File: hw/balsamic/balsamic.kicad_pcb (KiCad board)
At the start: 4 copper layers, 17.6 x 28.6 mm, 54 parts, among them J2 AXT524124, J3 USB_B_Micro, U1 BMI270, U2 MAX77651BEWVA+T, U3 ISP1807-LR-RS

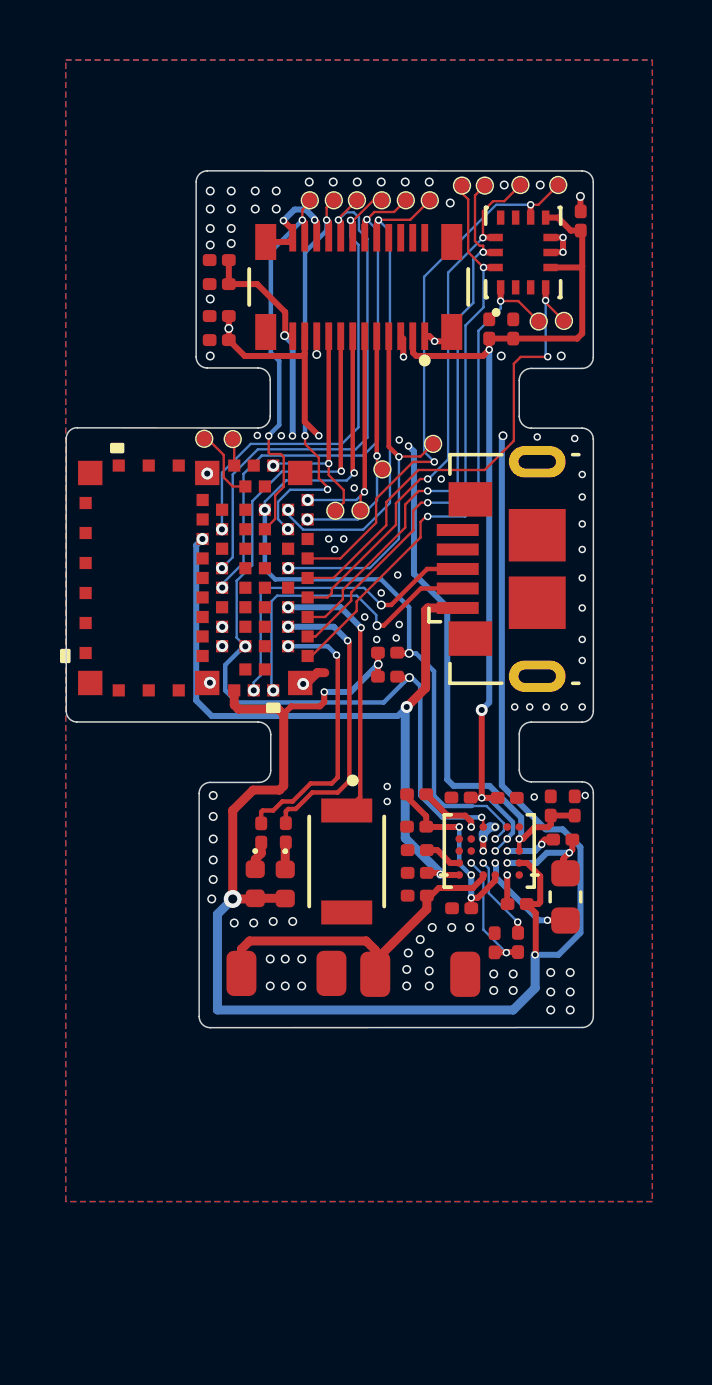
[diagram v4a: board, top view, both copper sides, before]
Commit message: incorporated Malik's board feedback
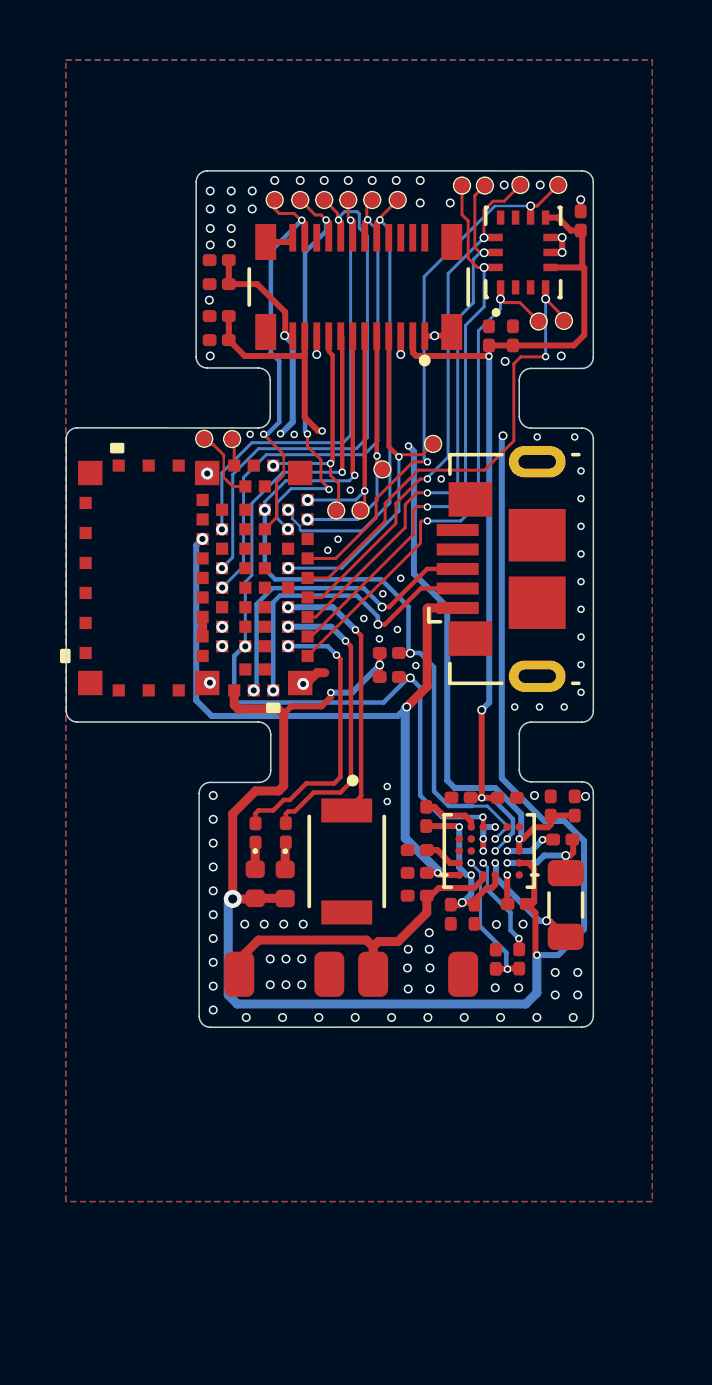
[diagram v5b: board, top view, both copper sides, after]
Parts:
- L1: footprint Inductor_SMD:L_0603_1608Metric -> Inductor_SMD:L_0805_2012Metric
- moved C1 3.50 mm to (76.1, 78.4), turned to -90 degrees
- moved TP17 1.17 mm to (69.5, 54.6)
- moved TP16 1.12 mm to (70.3, 54.6)
- moved TP13 1.12 mm to (72.7, 54.6)
- moved TP14 1.12 mm to (71.9, 54.6)
- moved TP15 1.09 mm to (71.1, 54.6)
- moved TP12 1.07 mm to (73.5, 54.6)
- moved R2 0.81 mm to (74.5, 75.2), turned to 90 degrees
- moved R5 0.55 mm to (77.6, 79.9)
- moved R3 0.55 mm to (76.8, 79.9)
- moved C11 0.41 mm to (75.3, 78.4), turned to -90 degrees
- moved L1 0.27 mm to (79.2, 78.1)
- moved C10 0.23 mm to (77.4, 59.1)
- moved C14 0.23 mm to (76.6, 59.1)
- moved R6 0.19 mm to (68.8, 75.7)
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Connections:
- net nRF_P0_02 renamed IMU_INT1
- net nRF_P0_15 renamed BUTTON
- net nRF_P0_31 renamed IMU_INT2
- U3 pad 20: GND -> Net-(U3-Pad20)
- U3 pad 22: GND -> Net-(U3-Pad20)
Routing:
- net GND: track 10.2 -> 7.30 mm, vias 111 -> 115
- net PMU_VSBB1: track 69.4 -> 68.1 mm, vias 7 -> 6
- net DVP_D3: track 16.4 -> 15.4 mm
- net DVP_D2: track 18.8 -> 17.9 mm
- net Net-(U3-Pad20): track 0.00 -> 0.65 mm
- net PMU_VSBB0: track 29.8 -> 30.5 mm
- net DVP_D1: track 16.1 -> 15.4 mm
- net DVP_MCLK: track 13.1 -> 13.7 mm
- net Net-(R5-Pad2): track 2.81 -> 3.38 mm
- net Net-(R3-Pad1): track 4.27 -> 4.83 mm
- net BATT: track 11.9 -> 11.3 mm
- net DVP_TRIG: track 12.3 -> 11.8 mm
- net DVP_SDA: track 28.8 -> 28.3 mm
- net Net-(R2-Pad2): track 2.06 -> 1.88 mm, vias 1 -> 0
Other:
- board size 17.6 x 28.6 mm -> 17.6 x 28.5 mm
